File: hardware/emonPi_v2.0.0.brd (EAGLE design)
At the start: 91.4 x 91.3 mm, 0 parts

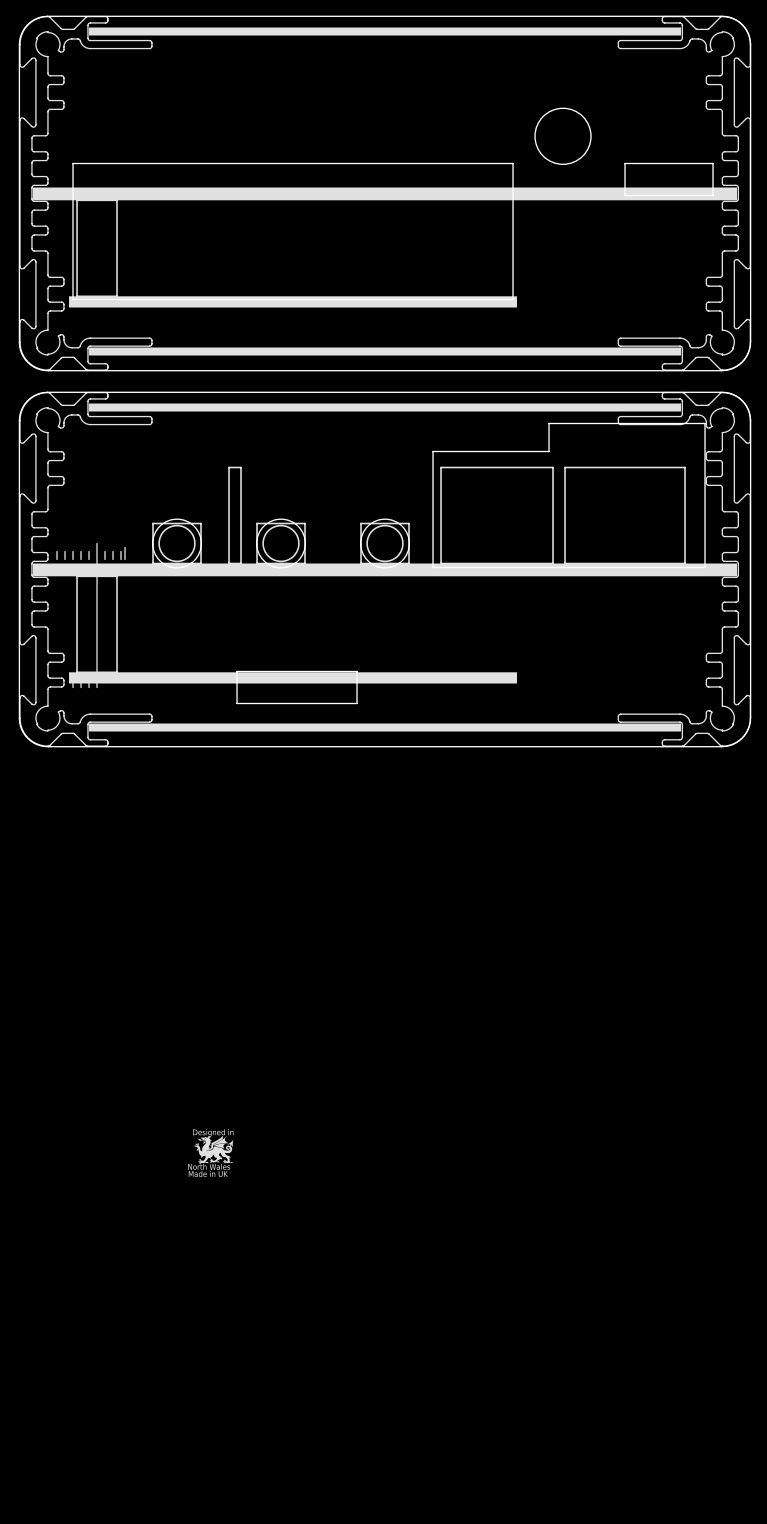
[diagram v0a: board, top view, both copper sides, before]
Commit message: emonPi v2 redesigned to use AVR128DB48++
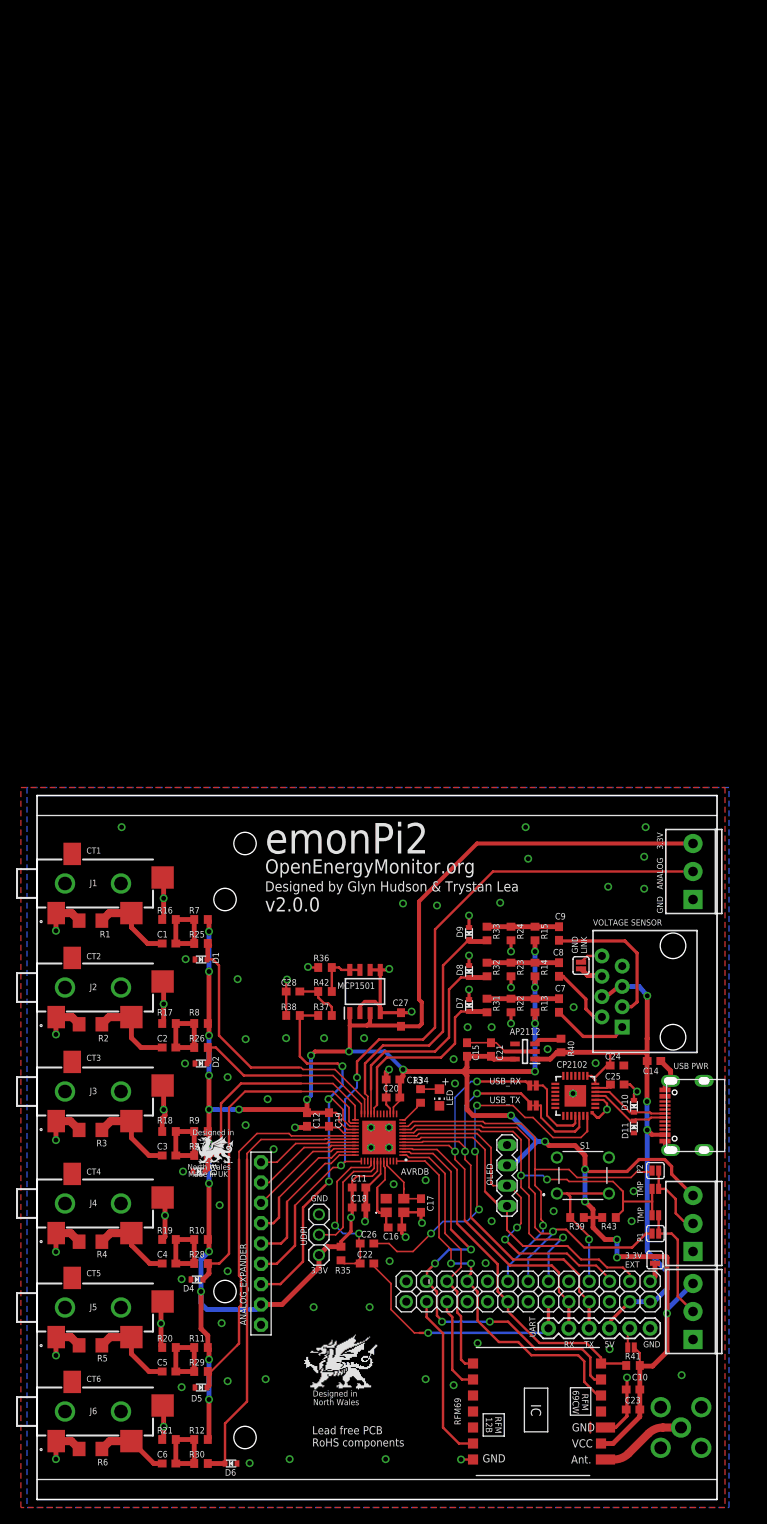
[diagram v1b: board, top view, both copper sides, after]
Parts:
- added 3V3_LINK, GND_LINK, SL2, SL4: SOLDERJUMPERNC, SparkFun:SJ_2S
- added ANALOG_EXPANDER: (no value), adafruit:1X09-BIG
- added AP2112: AP2112K-3.3TRG1, AP2112K-3.3TRG1:SOT95P282X130-5N
- added AVRDB: AVR128DB48T-E_6LX, AVR128DB48T-E_6LX:QFN40P600X600X90-49N
- added C1, C2, C3, C4, C5, C6, C7, C8, C9: 10uF 6V, resistor:C0603
- added C10: 10uF 6V, rcl:C0603
- added C11, C12, C13, C14, C15: 1uF 6V, resistor:C0603
- added C16, C17: 22pF, resistor:C0603
- added C18, C19, C20, C21, C22, C24, C25: 100nF, resistor:C0603
- added C23, C26: 100nF, rcl:C0603
- added C27, C28: 2.2uF, rcl:C0603
- added CN1, CN2, CN3: (no value), SparkFun-Connectors:SCREWTERMINAL-3.5MM-3
- added CP2102: CP210X_USB_UART, SparkFun-DigitalIC:MLP28
- added D1, D10, D11, D2, D3, D4, D5, D6, D7, D8, D9: ESD, microbuilder:SOD-523
- added J1, J2, J3, J4, J5, J6: SJ-3524-SMT-TR, SJ-3524-SMT-TR:SJ-3524-SMT-TR
- added JP1: 6x1, SparkFun:FTDI_BASIC
- added JP5, JP6: (no value), adafruit:1X13-BIG
- added LED: Red 1.85V, adafruit:CHIP-LED0805
- added MCP1501: MCP1501-10E_SN, MCP1501-10E_SN:SOIC127P600X175-8N
- added OLED: (no value), con-lstb-db:MA04-1
- added R1, R2, R3, R4, R5, R6: 1M, rcl:R1206
- added R10, R11, R12, R13, R14, R15, R7, R8, R9: 180k, rcl:R0603
- added R16, R17, R18, R19, R20, R21, R22, R23, R24: 33k, rcl:R0603
- added R25, R26, R27, R28, R29, R30, R31, R32, R33, R34: 1k, rcl:R0603
- added R35, R36, R37, R38, R39, R40: 10k, rcl:R0603
- added R41: 120k, rcl:R0603
- added R42: 10R, rcl:R0603
- added R43: 4K7, rcl:R0603
- added RFM69: RFM12B/69CW, eagle_jeelabs:RFM12B/69CW
- added RJ45: RJ45-8PTH, SparkFun-Connectors:RJ45-8
- added S1: 2-1825910-7, 2-1825910-7:218259107
- added SL1, SL3, UART_3.3, USB_RX, USB_TX: JUMPER-SMT_2_NC_PASTE_NO-SILK, SparkFun-Jumpers:SMT-JUMPER_2_NC_PASTE_NO-SILK
- added SMA: (no value), adafruit:SMA90_DIP
- added UDPI: (no value), adafruit:1X03
- added USB-C: CSP-USC16-TR, CSP-USC16-TR:USB-C
- added XTAL: MCSJK-7U-12.00-12-10-80-B-10, MCSJK-7U-12.00-12-10-80-B-10:MCSJK7U1200121080B10
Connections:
- new net +5V: AP2112.1, C14.2, C24.2, CP2102.7, CP2102.8, JP1.VCC, JP5.1, JP5.2, R40.1, RJ45.4, RJ45.5, USB-C.A4/B9
- new net 3.3V: 3V3_LINK.1, ANALOG_EXPANDER.2, AP2112.5, AVRDB.14, AVRDB.28, AVRDB.42, C10.1, C11.1, C12.1, C13.1, C15.2, C18.1, C19.1, C20.1, C21.2, C23.1, C27.1, CN1.3, CN2.3, CN3.3, MCP1501.1, MCP1501.3, OLED.3, R10.2, R11.2, R12.2, R13.2, R14.2, R15.2, R35.2, R39.1, R41.2, R43.1, R7.2, R8.2, R9.2, RFM69.VDD, UART_3.3.1, UDPI.3
- new net ANALOG_INPUT: ANALOG_EXPANDER.4, AVRDB.37, CN3.2
- new net AVR_RX: AVRDB.5, JP1.TXO, JP5.4, USB_TX.2
- new net AVR_TX: AVRDB.4, JP1.RXI, JP5.5, USB_RX.2
- new net CT1: AVRDB.23, D1.K, R25.2
- new net CT10: ANALOG_EXPANDER.6, AVRDB.35
- new net CT11: ANALOG_EXPANDER.5, AVRDB.36
- new net CT2: AVRDB.24, D2.K, R26.2
- new net CT3: AVRDB.25, D3.K, R27.1
- new net CT4: AVRDB.26, D4.K, R28.1
- new net CT5: AVRDB.30, D5.K, R29.1
- new net CT6: AVRDB.31, D6.K, R30.1
- new net CT7: ANALOG_EXPANDER.9, AVRDB.32
- new net CT8: ANALOG_EXPANDER.8, AVRDB.33
- new net CT9: ANALOG_EXPANDER.7, AVRDB.34
- new net D+: CP2102.4, D11.K, USB-C.A6
- new net D-: CP2102.5, D10.K, USB-C.A7
- new net DIG1: RFM69.ANT, SMA.ANTENNA
- new net DS18B20: AVRDB.8, JP6.6, R43.2, SL1.1, SL3.1
- new net DTR: C26.1, CP2102.28
- new net GND: ANALOG_EXPANDER.1, AP2112.2, AVRDB.15, AVRDB.29, AVRDB.43, AVRDB.49, C10.2, C11.2, C12.2, C13.2, C14.1, C15.1, C16.1, C17.2, C18.2, C19.2, C20.2, C21.1, C23.2, C24.1, C25.1, C27.2, C28.2, CN1.1, CN2.1, CN3.1, CP2102.3, CP2102.EXP, CP2102.M, D1.A, D10.A, D11.A, D2.A, D3.A, D4.A, D5.A, D6.A, D7.A, D8.A, D9.A, GND_LINK.1, J1.1, J1.4, J2.1, J2.4, J3.1, J3.4, J4.1, J4.4, J5.1, J5.4, J6.1, J6.4, JP1.GND, JP5.10, JP5.3, JP5.7, JP6.5, LED.C, MCP1501.2, MCP1501.4, MCP1501.5, MCP1501.6, OLED.4, R1.1, R16.2, R17.2, R18.2, R19.2, R2.1, R20.2, R21.2, R22.2, R23.1, R24.1, R3.1, R36.1, R38.1, R4.1, R5.1, R6.1, RFM69.GND, RFM69.GND1, RJ45.7, RJ45.8, S1.2, S1.4, SMA.GND1, SMA.GND2, SMA.GND3, SMA.GND4, UDPI.1, USB-C.A1/B12, USB-C.B1/A12, USB-C.GND1, USB-C.GND2, USB-C.GND3, USB-C.GND4, XTAL.2, XTAL.4
- new net LCD_BUTTON: JP6.4, R39.2, S1.1, S1.3
- new net LED: AVRDB.12, R34.2
- new net N$1: C1.1, J1.2, R1.2
- new net N$12: C9.2, R15.1, R24.2, R33.2
- new net N$13: C2.1, J2.2, R2.2
- new net N$14: C5.1, J5.2, R5.2
- new net N$15: C5.2, R11.1, R20.1, R29.2
- new net N$16: C2.2, R17.1, R26.1, R8.1
- new net N$17: C4.2, R10.1, R19.1, R28.2
- new net N$18: C1.2, R16.1, R25.1, R7.1
- new net N$19: C6.1, J6.2, R6.2
- new net N$2: C7.2, R13.1, R22.1, R31.2
- new net N$20: C6.2, R12.1, R21.1, R30.2
- new net N$21: C3.2, R18.1, R27.2, R9.1
- new net N$22: CN1.2, SL1.2, SL2.2
- new net N$23: CN2.2, SL3.2, SL4.2
- new net N$24: GND_LINK.2, RJ45.6
- new net N$25: AP2112.3, R40.2
- new net N$26: C28.1, R37.2, R42.1
- new net N$27: MCP1501.7, MCP1501.8, R36.2, R42.2
- new net N$28: 3V3_LINK.2, JP6.1
- new net N$3: C3.1, J3.2, R3.2
- new net N$31: C25.2, CP2102.6
- new net N$33: JP1.CTS, UART_3.3.2
- new net N$4: C8.2, R14.1, R23.2, R32.2
- new net N$41: LED.A, R34.1
- new net N$5: C4.1, J4.2, R4.2
- new net PULSE1: AVRDB.9, JP6.7, SL4.1
- new net PULSE2: AVRDB.10, JP6.8, SL2.1
- new net RESET: AVRDB.40, C22.2, C26.2, R35.1
- new net RFM_IRQ: JP5.11, RFM69.IRQ
- new net RFM_MISO: AVRDB.1, JP6.11, RFM69.SDO
- new net RFM_MOSI: AVRDB.48, JP6.10, RFM69.SDI
- new net RFM_RESET: JP5.12, RFM69.RST
- new net RFM_SCK: AVRDB.2, JP6.12, RFM69.SCK
- new net RFM_SEL: AVRDB.3, JP5.8, R41.1, RFM69.SEL
- new net SCL: AVRDB.7, JP6.3, OLED.2
- new net SDA: AVRDB.6, JP6.2, OLED.1
- new net UDPI: AVRDB.41, UDPI.2
- new net USB_RXD: CP2102.25, USB_RX.1
- new net USB_TXD: CP2102.26, USB_TX.1
- new net VREFA: ANALOG_EXPANDER.3, AVRDB.27, R37.1, R38.2
- new net VS1: C7.1, RJ45.1
- new net VS2: C8.1, RJ45.2
- new net VS3: C9.1, RJ45.3
- new net VSENS1: AVRDB.20, D7.K, R31.1
- new net VSENS2: AVRDB.21, D8.K, R32.1
- new net VSENS3: AVRDB.22, D9.K, R33.1
- new net XTAL1: AVRDB.44, C16.2, XTAL.1
- new net XTAL2: AVRDB.45, C17.1, XTAL.3
- new net _RESET: C22.1, JP1.DTR, JP5.6
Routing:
- net 3.3V: track 0.00 -> 366.0 mm, vias 0 -> 28
- net GND: track 0.00 -> 168.6 mm, vias 0 -> 90
- net ANALOG_INPUT: track 0.00 -> 93.6 mm, vias 0 -> 2
- net +5V: track 0.00 -> 77.0 mm, vias 0 -> 3
- net DS18B20: track 0.00 -> 62.8 mm, vias 0 -> 3
- net CT6: track 0.00 -> 56.6 mm
- net AVR_RX: track 0.00 -> 56.2 mm, vias 0 -> 2
- net RFM_SCK: track 0.00 -> 55.8 mm, vias 0 -> 4
- net AVR_TX: track 0.00 -> 55.1 mm, vias 0 -> 2
- net PULSE2: track 0.00 -> 53.2 mm, vias 0 -> 1
- net PULSE1: track 0.00 -> 52.4 mm, vias 0 -> 1
- net VREFA: track 0.00 -> 52.0 mm, vias 0 -> 3
- net RFM_MOSI: track 0.00 -> 48.9 mm, vias 0 -> 2
- net CT5: track 0.00 -> 47.7 mm
- net DTR: track 0.00 -> 47.0 mm, vias 0 -> 4
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- added copper zone on layer 1, net GND
- added copper zone on layer 16, net GND
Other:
- board size 91.4 x 91.3 mm -> 85 x 88 mm
- board text added: "3.3V"
- board text added: "3.3V EXT"
- board text added: "5V"
- board text added: "ANALOG"
- board text added: "CT1"
- board text added: "CT2"
- board text added: "CT3"
- board text added: "CT4"
- board text added: "CT5"
- board text added: "CT6"
- board text added: "Designed by Glyn Hudson & Trystan Lea"
- board text added: "GND"
- board text added: "GND LINK"
- board text added: "Lead free PCB RoHS components"
- board text added: "OpenEnergyMonitor.org"
- board text added: "P1"
- board text added: "P2"
- board text added: "RX"
- board text added: "TMP"
- board text added: "TX"
- board text added: "UART"
- board text added: "USB PWR"
- board text added: "VOLTAGE SENSOR"
- board text added: "emonPi2"
- board text added: "v2.0.0"

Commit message: export
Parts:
- added FD1, FD2, FD3: FIDUCIAL1X2, SparkFun-Aesthetics:FIDUCIAL-1X2
- added LOGO1: OSHW-LOGOS-COPPER, SparkFun-Aesthetics:OSHW-LOGO-S_COPPER
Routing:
- net GND: vias 90 -> 91
